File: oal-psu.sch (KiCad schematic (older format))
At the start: 62 parts, among them J1 MAINS_LINE, J2 MAINS_NEUTRAL, J3 OUTPUT, P101 ENABLE_A, P2 OUTPUT_SELECT, P201 ENABLE_B, SW1 DPDT_SLIDE, SW102 VOLTAGE_A, SW202 VOLTAGE_B, T1 TALEMA 15/25VA, U101 TPS7A4700, U201 TPS7A4700, X1 M3 HOLE, X2 M3 HOLE, X3 M3 HOLE, X4 M3 HOLE, X5 M3 HOLE

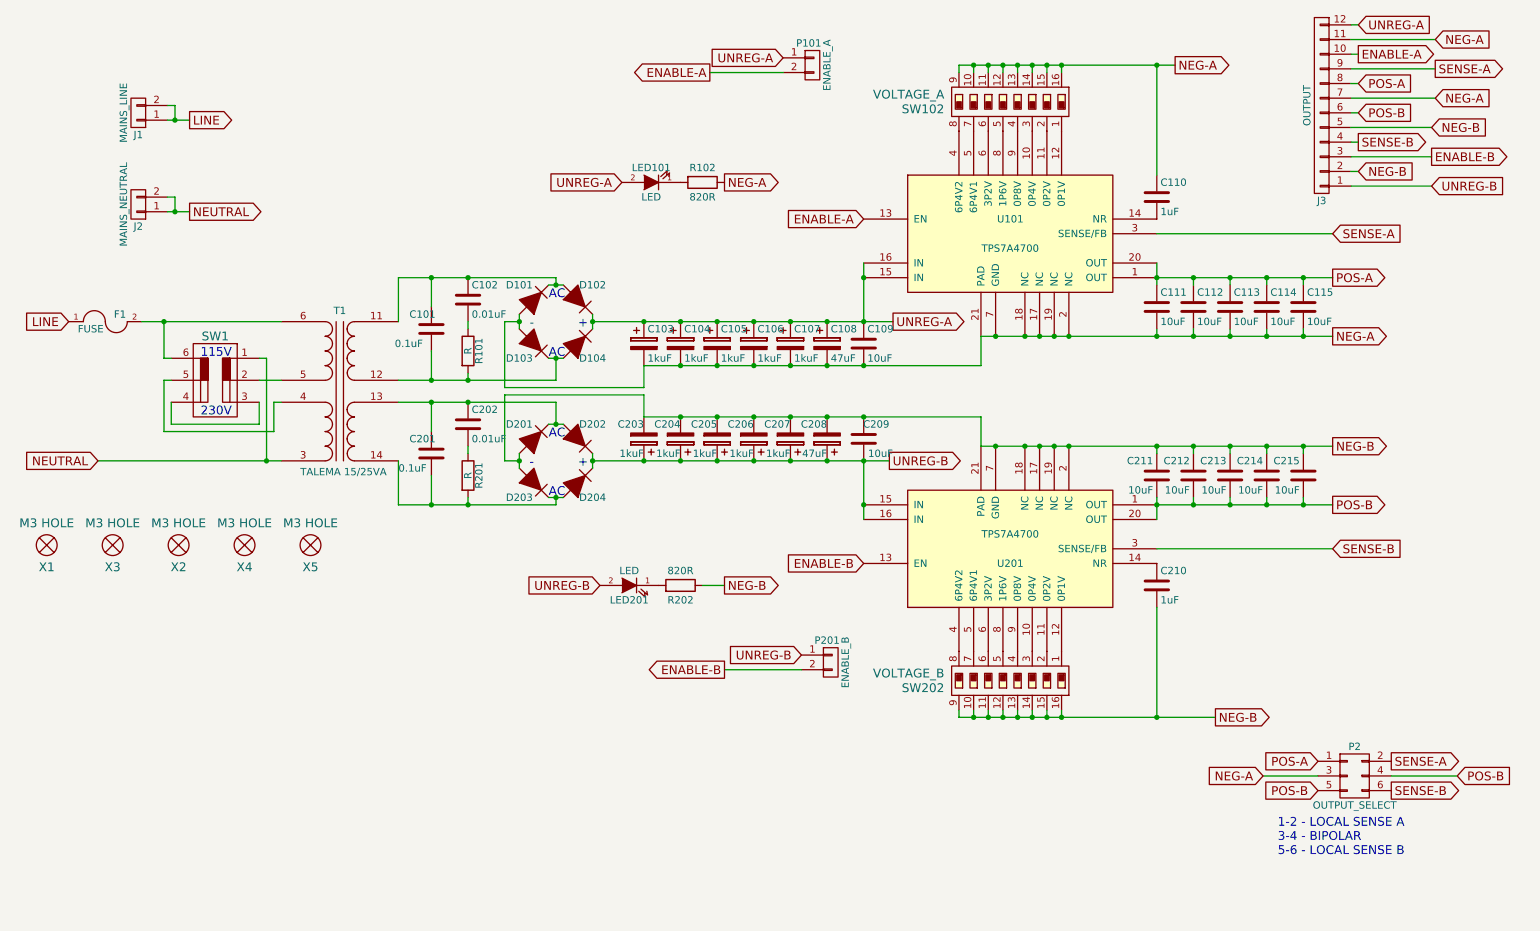
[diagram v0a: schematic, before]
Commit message: new output connectors
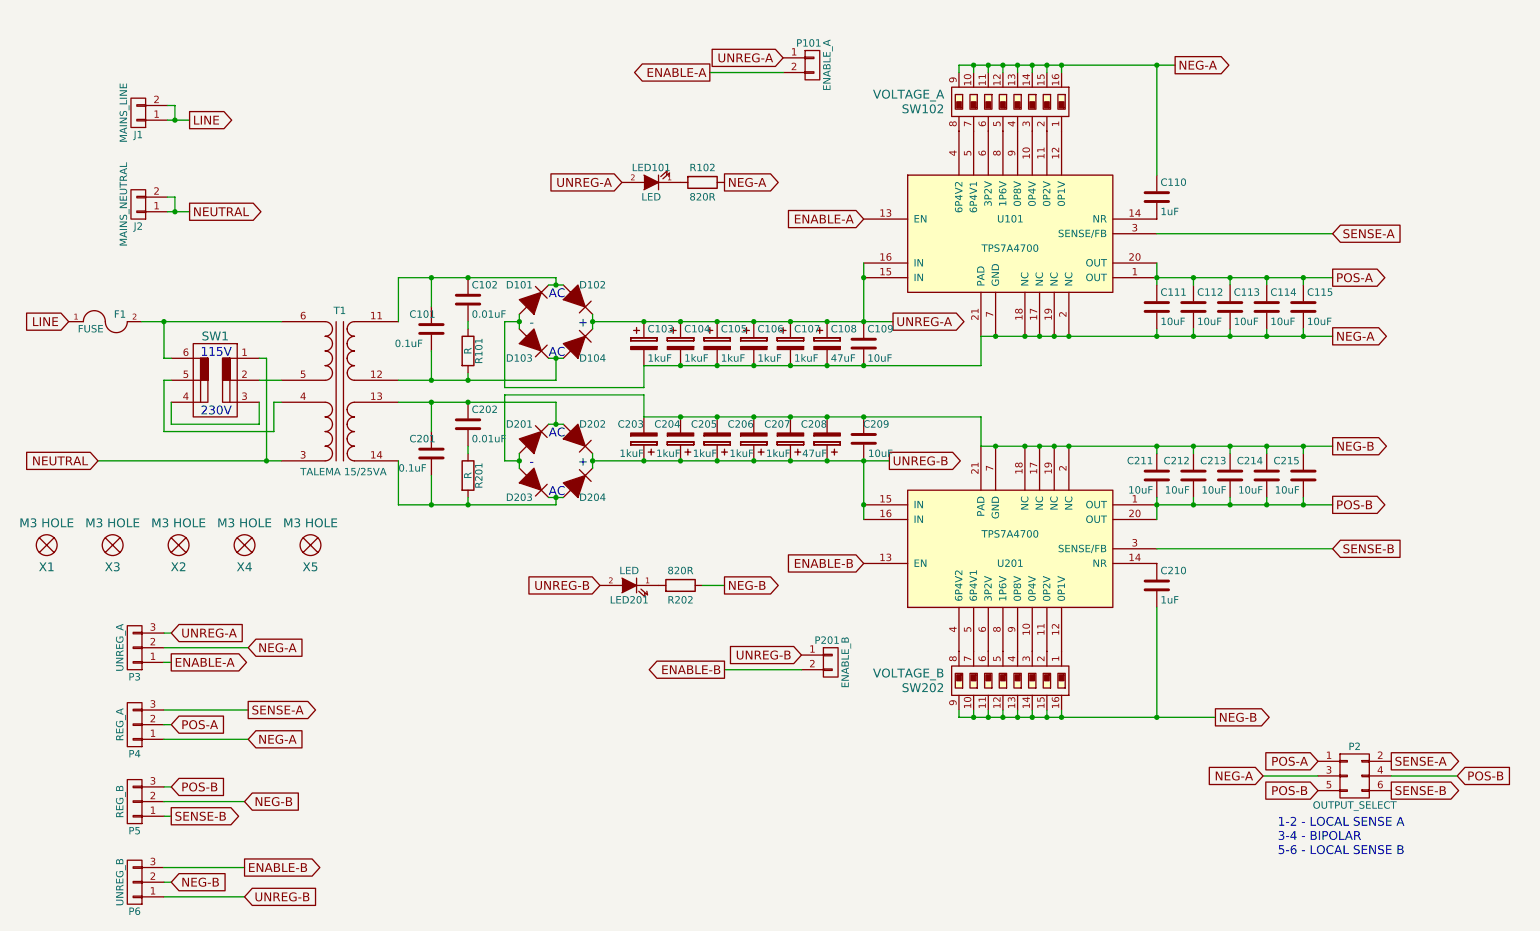
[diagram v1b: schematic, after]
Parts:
- removed J3: OUTPUT, ose-audio-labs:PHEONIX_MC1.5-12-G-3.5, symbol CONN_01X12
- added P3: UNREG_A, ose-audio-labs:Phoenix-PTSM-0,5-3, symbol CONN_01X03
- added P4: REG_A, ose-audio-labs:Phoenix-PTSM-0,5-3, symbol CONN_01X03
- added P5: REG_B, ose-audio-labs:Phoenix-PTSM-0,5-3, symbol CONN_01X03
- added P6: UNREG_B, ose-audio-labs:Phoenix-PTSM-0,5-3, symbol CONN_01X03
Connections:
- net ENABLE-A: now also P3.1 (P1)
- net ENABLE-B: now also P6.3 (P3)
- net NEG-A: now also P3.2 (P2), P4.1 (P1)
- net NEG-B: now also P5.2 (P2), P6.2 (P2)
- net POS-A: now also P4.2 (P2)
- net POS-B: now also P5.3 (P3)
- net SENSE-A: now also P4.3 (P3)
- net SENSE-B: now also P5.1 (P1)
- net UNREG-A: now also P3.3 (P3)
- net UNREG-B: now also P6.1 (P1)
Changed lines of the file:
@@
 Text GLabel 8900 5400 2    60   Output ~ 0
 NEG-B
-$Comp
-L CONN_01X02 J2
-U 1 1 56C3204B
-P 1550 1900
-F 0 "J2" H 1550 2050 50  0000 C CNN
-F 1 "MAINS_NEUTRAL" V 1650 1900 50  0000 C CNN
-F 2 "ose-audio-labs:PHEONIX_SPT_5-2POS" H 1550 1900 50  0001 C CNN
-F 3 "" H 1550 1900 50  0000 C CNN
-	1    1550 1900
-	-1   0    0    1
-$EndComp
 Text GLabel 1900 1950 2    60   Output ~ 0
 NEUTRAL
-Text GLabel 9875 1075 2    60   Input ~ 0
+Text GLabel 1775 5450 2    60   Input ~ 0
 POS-A
-Text GLabel 10400 1175 2    60   Input ~ 0
+Text GLabel 2300 5550 2    60   Input ~ 0
 NEG-A
-Text GLabel 9875 1275 2    60   Input ~ 0
+Text GLabel 1775 5875 2    60   Input ~ 0
 POS-B
-Text GLabel 10375 1375 2    60   Input ~ 0
+Text GLabel 2275 5975 2    60   Input ~ 0
 NEG-B
 $Comp
@@
 Text GLabel 9700 4250 2    60   Input ~ 0
 SENSE-B
-Text GLabel 10400 975  2    60   Output ~ 0
+Text GLabel 2300 5350 2    60   Output ~ 0
 SENSE-A
-Text GLabel 9875 1475 2    60   Output ~ 0
+Text GLabel 1775 6075 2    60   Output ~ 0
 SENSE-B
 Text GLabel 10100 5700 2    60   Output ~ 0
@@
 	1    0    0    -1
 $EndComp
-$Comp
-L CONN_01X02 J1
-U 1 1 56CFDE2E
-P 1550 1275
-F 0 "J1" H 1550 1425 50  0000 C CNN
-F 1 "MAINS_LINE" V 1650 1275 50  0000 C CNN
-F 2 "ose-audio-labs:PHEONIX_SPT_5-2POS" H 1550 1275 50  0001 C CNN
-F 3 "" H 1550 1275 50  0000 C CNN
-	1    1550 1275
-	-1   0    0    1
-$EndComp
 Text GLabel 1900 1325 2    60   Output ~ 0
 LINE
@@
 Text GLabel 6700 2700 2    60   Output ~ 0
 UNREG-A
-Text GLabel 9875 675  2    60   Input ~ 0
+Text GLabel 1775 4825 2    60   Input ~ 0
 UNREG-A
-Text GLabel 9875 875  2    60   Output ~ 0
+Text GLabel 1775 5025 2    60   Output ~ 0
 ENABLE-A
-Text GLabel 10400 775  2    60   Input ~ 0
+Text GLabel 2300 4925 2    60   Input ~ 0
 NEG-A
 Text GLabel 6500 2000 0    60   Input ~ 0
@@
 Text GLabel 5450 1000 0    60   Output ~ 0
 ENABLE-A
-$Comp
-L CONN_01X12 J3
-U 1 1 56D31B65
-P 9625 1225
-F 0 "J3" H 9625 1875 50  0000 C CNN
-F 1 "OUTPUT" V 9725 1225 50  0000 C CNN
-F 2 "ose-audio-labs:PHEONIX_MC1.5-12-G-3.5" H 9625 1225 50  0001 C CNN
-F 3 "" H 9625 1225 50  0000 C CNN
-	1    9625 1225
-	-1   0    0    1
-$EndComp
-Text GLabel 9875 1675 2    60   Input ~ 0
+Text GLabel 1775 6525 2    60   Input ~ 0
 NEG-B
-Text GLabel 10375 1775 2    60   Input ~ 0
+Text GLabel 2275 6625 2    60   Input ~ 0
 UNREG-B
-Text GLabel 10375 1575 2    60   Output ~ 0
+Text GLabel 2275 6425 2    60   Output ~ 0
 ENABLE-B
 Connection ~ 4150 3650
@@
 Connection ~ 6500 3000
 Wire Wire Line
-	9825 1175 10400 1175
+	1725 5550 2300 5550
 Wire Wire Line
 	1750 1950 1900 1950
@@
 Connection ~ 6500 2400
 Wire Wire Line
-	9825 675  9875 675
-Wire Wire Line
-	9825 775  10400 775
-Wire Wire Line
-	9825 875  9875 875
-Wire Wire Line
-	9825 975  10400 975
-Wire Wire Line
-	9825 1075 9875 1075
-Wire Wire Line
-	9825 1275 9875 1275
-Wire Wire Line
-	9825 1375 10375 1375
-Wire Wire Line
-	9825 1475 9875 1475
-Wire Wire Line
-	9825 1575 10375 1575
-Wire Wire Line
-	9825 1675 9875 1675
-Wire Wire Line
-	10375 1775 9825 1775
+	1725 4825 1775 4825
+Wire Wire Line
+	1725 4925 2300 4925
+Wire Wire Line
+	1725 5025 1775 5025
+Wire Wire Line
+	1725 5350 2300 5350
+Wire Wire Line
+	1725 5450 1775 5450
+Wire Wire Line
+	1725 5875 1775 5875
+Wire Wire Line
+	1725 5975 2275 5975
+Wire Wire Line
+	1725 6075 1775 6075
+Wire Wire Line
+	1725 6425 2275 6425
+Wire Wire Line
+	1725 6525 1775 6525
+Wire Wire Line
+	2275 6625 1725 6625
 Wire Wire Line
 	5450 1000 5950 1000
@@
 	1    0    0    -1
 $EndComp
+$Comp
+L CONN_01X02 J2
+U 1 1 56C3204B
+P 1550 1900
+F 0 "J2" H 1550 2050 50  0000 C CNN
+F 1 "MAINS_NEUTRAL" V 1650 1900 50  0000 C CNN
+F 2 "ose-audio-labs:PHEONIX_SPT_5-2POS" H 1550 1900 50  0001 C CNN
+F 3 "" H 1550 1900 50  0000 C CNN
+	1    1550 1900
+	-1   0    0    1
+$EndComp
+$Comp
+L CONN_01X02 J1
+U 1 1 56CFDE2E
+P 1550 1275
+F 0 "J1" H 1550 1425 50  0000 C CNN
+F 1 "MAINS_LINE" V 1650 1275 50  0000 C CNN
+F 2 "ose-audio-labs:PHEONIX_SPT_5-2POS" H 1550 1275 50  0001 C CNN
+F 3 "" H 1550 1275 50  0000 C CNN
+	1    1550 1275
+	-1   0    0    1
+$EndComp
+$Comp
+L CONN_01X03 P3
+U 1 1 56DF9A8B
+P 1525 4925
+F 0 "P3" H 1525 5125 50  0000 C CNN
+F 1 "UNREG_A" V 1625 4925 50  0000 C CNN
+F 2 "ose-audio-labs:Phoenix-PTSM-0,5-3" H 1525 4925 50  0001 C CNN
+F 3 "" H 1525 4925 50  0000 C CNN
+	1    1525 4925
+	-1   0    0    1
+$EndComp
+$Comp
+L CONN_01X03 P6
+U 1 1 56DF9C02
+P 1525 6525
+F 0 "P6" H 1525 6725 50  0000 C CNN
+F 1 "UNREG_B" V 1625 6525 50  0000 C CNN
+F 2 "ose-audio-labs:Phoenix-PTSM-0,5-3" H 1525 6525 50  0001 C CNN
+F 3 "" H 1525 6525 50  0000 C CNN
+	1    1525 6525
+	-1   0    0    1
+$EndComp
+$Comp
+L CONN_01X03 P4
+U 1 1 56DF9FAE
+P 1525 5450
+F 0 "P4" H 1525 5650 50  0000 C CNN
+F 1 "REG_A" V 1625 5450 50  0000 C CNN
+F 2 "ose-audio-labs:Phoenix-PTSM-0,5-3" H 1525 5450 50  0001 C CNN
+F 3 "" H 1525 5450 50  0000 C CNN
+	1    1525 5450
+	-1   0    0    1
+$EndComp
+$Comp
+L CONN_01X03 P5
+U 1 1 56DFA0B5
+P 1525 5975
+F 0 "P5" H 1525 6175 50  0000 C CNN
+F 1 "REG_B" V 1625 5975 50  0000 C CNN
+F 2 "ose-audio-labs:Phoenix-PTSM-0,5-3" H 1525 5975 50  0001 C CNN
+F 3 "" H 1525 5975 50  0000 C CNN
+	1    1525 5975
+	-1   0    0    1
+$EndComp
 $EndSCHEMATC

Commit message: layout updates
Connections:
- net ENABLE-A: now also P3.3 (P3); no longer P3.1 (P1)
- net NEG-B: now also P5.1 (P1); no longer P5.2 (P2)
- net POS-B: now also P5.2 (P2); no longer P5.3 (P3)
- net SENSE-B: now also P5.3 (P3); no longer P5.1 (P1)
- net UNREG-A: now also P3.1 (P1); no longer P3.3 (P3)
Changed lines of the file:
@@
 Text GLabel 1900 1950 2    60   Output ~ 0
 NEUTRAL
-Text GLabel 1775 5450 2    60   Input ~ 0
+Text GLabel 2225 5450 2    60   Input ~ 0
 POS-A
-Text GLabel 2300 5550 2    60   Input ~ 0
+Text GLabel 1775 5550 2    60   Input ~ 0
 NEG-A
-Text GLabel 1775 5875 2    60   Input ~ 0
+Text GLabel 2225 5975 2    60   Input ~ 0
 POS-B
-Text GLabel 2275 5975 2    60   Input ~ 0
+Text GLabel 1775 6075 2    60   Input ~ 0
 NEG-B
 $Comp
@@
 Text GLabel 9700 4250 2    60   Input ~ 0
 SENSE-B
-Text GLabel 2300 5350 2    60   Output ~ 0
+Text GLabel 1775 5350 2    60   Output ~ 0
 SENSE-A
-Text GLabel 1775 6075 2    60   Output ~ 0
+Text GLabel 1775 5875 2    60   Output ~ 0
 SENSE-B
 Text GLabel 10100 5700 2    60   Output ~ 0
@@
 Text GLabel 6700 2700 2    60   Output ~ 0
 UNREG-A
-Text GLabel 1775 4825 2    60   Input ~ 0
+Text GLabel 1775 5025 2    60   Input ~ 0
 UNREG-A
-Text GLabel 1775 5025 2    60   Output ~ 0
+Text GLabel 1775 4825 2    60   Output ~ 0
 ENABLE-A
 Text GLabel 2300 4925 2    60   Input ~ 0
@@
 Text GLabel 5450 1000 0    60   Output ~ 0
 ENABLE-A
-Text GLabel 1775 6525 2    60   Input ~ 0
+Text GLabel 2300 6525 2    60   Input ~ 0
 NEG-B
-Text GLabel 2275 6625 2    60   Input ~ 0
+Text GLabel 1775 6625 2    60   Input ~ 0
 UNREG-B
-Text GLabel 2275 6425 2    60   Output ~ 0
+Text GLabel 1775 6425 2    60   Output ~ 0
 ENABLE-B
 Connection ~ 4150 3650
@@
 Connection ~ 6500 3000
 Wire Wire Line
-	1725 5550 2300 5550
-Wire Wire Line
 	1750 1950 1900 1950
 Connection ~ 8500 2800
@@
 	1725 5025 1775 5025
 Wire Wire Line
-	1725 5350 2300 5350
-Wire Wire Line
-	1725 5450 1775 5450
+	1725 5450 2225 5450
 Wire Wire Line
 	1725 5875 1775 5875
 Wire Wire Line
-	1725 5975 2275 5975
-Wire Wire Line
 	1725 6075 1775 6075
-Wire Wire Line
-	1725 6425 2275 6425
-Wire Wire Line
-	1725 6525 1775 6525
-Wire Wire Line
-	2275 6625 1725 6625
 Wire Wire Line
 	5450 1000 5950 1000
@@
 	-1   0    0    1
 $EndComp
+Wire Wire Line
+	1725 5350 1775 5350
+Wire Wire Line
+	1725 5550 1775 5550
+Wire Wire Line
+	1725 5975 2225 5975
+Wire Wire Line
+	2300 6525 1725 6525
+Wire Wire Line
+	1725 6425 1775 6425
+Wire Wire Line
+	1725 6625 1775 6625
 $EndSCHEMATC
